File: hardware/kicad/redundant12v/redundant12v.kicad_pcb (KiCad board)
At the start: 2 copper layers, 27 parts, among them J1 Conn_01x06, J2 Conn_02x05_Odd_Even, Q1 2N3904, Q2 2N3904, U1 ATtiny212-SS, U2 MAX232CPE, U3 LD1117S50TR_SOT223, X1 ASCO

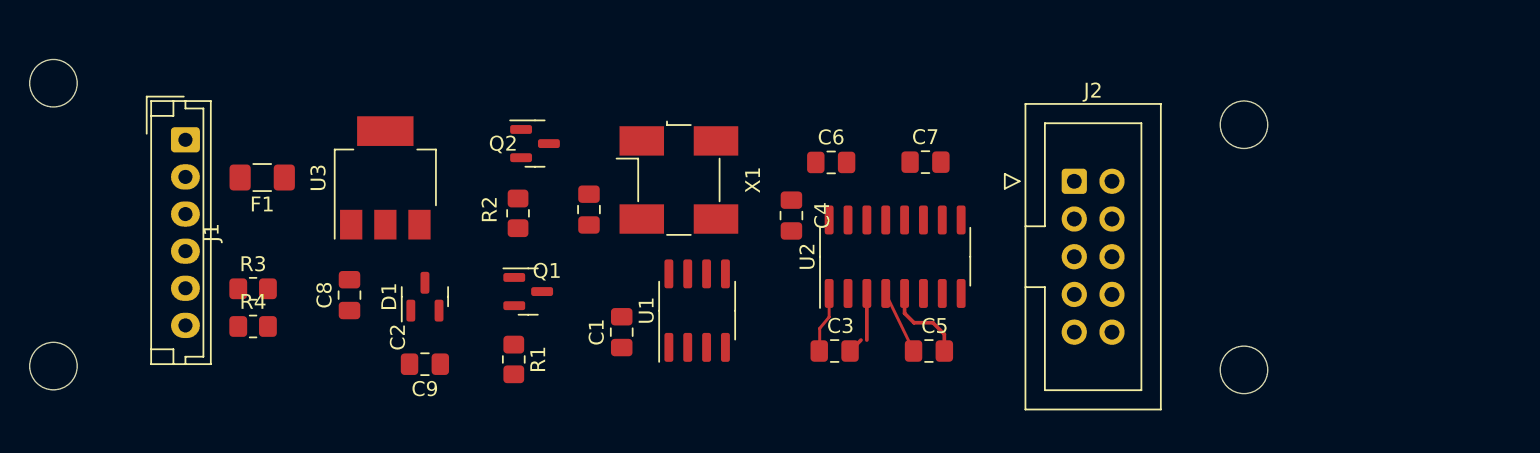
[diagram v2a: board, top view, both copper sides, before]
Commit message: Add serial port connections
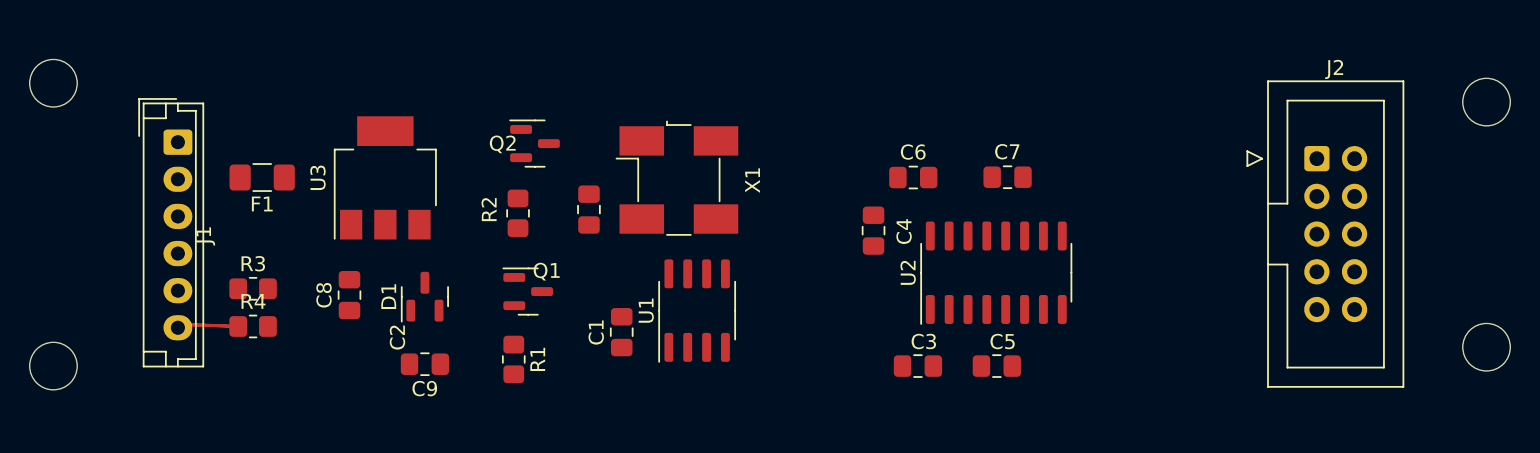
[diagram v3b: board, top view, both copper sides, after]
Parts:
- moved J2 16.4 mm to (189.2, 88.9)
- moved REF** 16.4 mm to (200.7, 85.1)
- moved REF** 16.4 mm to (200.7, 101.6)
- moved U2 6.90 mm to (167.6, 96.6)
- moved C3 5.70 mm to (162.4, 102.9)
- moved C4 5.62 mm to (159.4, 93.7)
- moved C6 5.62 mm to (162.1, 90.2)
- moved C7 5.62 mm to (168.4, 90.2)
- moved C5 4.68 mm to (167.7, 102.9)
- moved J1 0.53 mm to (112.5, 87.8)
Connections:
- net RX renamed RX_5V
- net TX renamed TX_5V
- U2 pad 13: unconnected-(U2-Pad13) -> RX_12V
- U2 pad 14: unconnected-(U2-Pad14) -> TX_12V
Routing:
- net Net-(C5-Pad2): track 5.73 -> 0.00 mm
- net Net-(C3-Pad2): track 4.18 -> 0.00 mm
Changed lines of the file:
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@@
   (net 0 "")
   (net 1 "VCC")
-  (net 2 "TX")
-  (net 3 "RX")
+  (net 2 "TX_5V")
+  (net 3 "RX_5V")
   (net 4 "EXTCLK")
   (net 5 "GND")
@@
   (net 14 "unconnected-(U2-Pad9)")
   (net 15 "unconnected-(U2-Pad10)")
-  (net 16 "unconnected-(U2-Pad13)")
-  (net 17 "unconnected-(U2-Pad14)")
+  (net 16 "RX_12V")
+  (net 17 "TX_12V")
   (net 18 "unconnected-(X1-Pad1)")
   (net 19 "PS0")
@@
   )
   (footprint "Capacitor_SMD:C_0805_2012Metric_Pad1.18x1.45mm_HandSolder" (layer "F.Cu")
-    (at 163.104 101.8545)
+    (at 167.6775 102.87)
     (descr "Capacitor SMD 0805 (2012 Metric), square (rectangular) end terminal, IPC_7351 nominal with elongated pad for handsoldering. (Body size source: IPC-SM-782 page 76, https://www.pcb-3d.com/wordpress/wp-content/uploads/ipc-sm-782a_amendment_1_and_2.pdf, https://docs.google.com/spreadsheets/d/1BsfQQcO9C6DZCsRaXUlFlo91Tg2WpOkGARC1WS5S8t0/edit?usp=sharing), generated with kicad-footprint-generator")
     (tags "capacitor handsolder")
@@
     (property "Sheetname" "")
     (attr smd)
-    (fp_text reference "C5" (at 0.395 -1.68) (layer "F.SilkS")
+    (fp_text reference "C5" (at 0.4105 -1.618) (layer "F.SilkS")
       (effects (font (size 1 1) (thickness 0.15)))
     )
@@
   )
   (footprint "Connector_JST:JST_EH_B6B-EH-A_1x06_P2.50mm_Vertical" (layer "F.Cu")
-    (at 113.03 87.63 -90)
+    (at 112.522 87.79 -90)
     (descr "JST EH series connector, B6B-EH-A (http://www.jst-mfg.com/product/pdf/eng/eEH.pdf), generated with kicad-footprint-generator")
     (tags "connector JST EH vertical")
@@
   )
   (footprint "Capacitor_SMD:C_0805_2012Metric_Pad1.18x1.45mm_HandSolder" (layer "F.Cu")
-    (at 156.5215 89.1545)
+    (at 162.052 90.17)
     (descr "Capacitor SMD 0805 (2012 Metric), square (rectangular) end terminal, IPC_7351 nominal with elongated pad for handsoldering. (Body size source: IPC-SM-782 page 76, https://www.pcb-3d.com/wordpress/wp-content/uploads/ipc-sm-782a_amendment_1_and_2.pdf, https://docs.google.com/spreadsheets/d/1BsfQQcO9C6DZCsRaXUlFlo91Tg2WpOkGARC1WS5S8t0/edit?usp=sharing), generated with kicad-footprint-generator")
     (tags "capacitor handsolder")
@@
       (net 1 "VCC") (pinfunction "VCC") (pintype "power_in"))
     (pad "2" smd roundrect (at -2.475 -0.635 90) (size 1.95 0.6) (layers "F.Cu" "F.Paste" "F.Mask") (roundrect_rratio 0.25)
-      (net 2 "TX") (pinfunction "PA6") (pintype "bidirectional"))
+      (net 2 "TX_5V") (pinfunction "PA6") (pintype "bidirectional"))
     (pad "3" smd roundrect (at -2.475 0.635 90) (size 1.95 0.6) (layers "F.Cu" "F.Paste" "F.Mask") (roundrect_rratio 0.25)
-      (net 3 "RX") (pinfunction "PA7") (pintype "bidirectional"))
+      (net 3 "RX_5V") (pinfunction "PA7") (pintype "bidirectional"))
     (pad "4" smd roundrect (at -2.475 1.905 90) (size 1.95 0.6) (layers "F.Cu" "F.Paste" "F.Mask") (roundrect_rratio 0.25)
       (net 19 "PS0") (pinfunction "PA1") (pintype "bidirectional"))
@@
   )
   (footprint "Package_SO:SOIC-16_3.9x9.9mm_P1.27mm" (layer "F.Cu")
-    (at 160.829 95.5045 90)
+    (at 167.64 96.582 90)
     (descr "SOIC, 16 Pin (JEDEC MS-012AC, https://www.analog.com/media/en/package-pcb-resources/package/pkg_pdf/soic_narrow-r/r_16.pdf), generated with kicad-footprint-generator ipc_gullwing_generator.py")
     (tags "SOIC SO")
@@
       (effects (font (size 1 1) (thickness 0.15)))
     )
-    (fp_text value "MAX232CPE" (at 0 5.9 90) (layer "F.Fab")
+    (fp_text value "MAX232CPE" (at 0 5.9375 90) (layer "F.Fab")
       (effects (font (size 1 1) (thickness 0.15)))
     )
@@
       (net 15 "unconnected-(U2-Pad10)") (pinfunction "T2IN") (pintype "input+no_connect"))
     (pad "11" smd roundrect (at 2.475 1.905 90) (size 1.95 0.6) (layers "F.Cu" "F.Paste" "F.Mask") (roundrect_rratio 0.25)
-      (net 2 "TX") (pinfunction "T1IN") (pintype "input"))
+      (net 2 "TX_5V") (pinfunction "T1IN") (pintype "input"))
     (pad "12" smd roundrect (at 2.475 0.635 90) (size 1.95 0.6) (layers "F.Cu" "F.Paste" "F.Mask") (roundrect_rratio 0.25)
-      (net 3 "RX") (pinfunction "R1OUT") (pintype "output"))
+      (net 3 "RX_5V") (pinfunction "R1OUT") (pintype "output"))
     (pad "13" smd roundrect (at 2.475 -0.635 90) (size 1.95 0.6) (layers "F.Cu" "F.Paste" "F.Mask") (roundrect_rratio 0.25)
-      (net 16 "unconnected-(U2-Pad13)") (pinfunction "R1IN") (pintype "input"))
+      (net 16 "RX_12V") (pinfunction "R1IN") (pintype "input"))
     (pad "14" smd roundrect (at 2.475 -1.905 90) (size 1.95 0.6) (layers "F.Cu" "F.Paste" "F.Mask") (roundrect_rratio 0.25)
-      (net 17 "unconnected-(U2-Pad14)") (pinfunction "T1OUT") (pintype "output"))
+      (net 17 "TX_12V") (pinfunction "T1OUT") (pintype "output"))
     (pad "15" smd roundrect (at 2.475 -3.175 90) (size 1.95 0.6) (layers "F.Cu" "F.Paste" "F.Mask") (roundrect_rratio 0.25)
       (net 5 "GND") (pinfunction "GND") (pintype "power_in"))
@@
   )
   (footprint "MountingHole:MountingHole_3.2mm_M3" (layer "F.Cu")
-    (at 184.324 86.6145)
+    (at 200.66 85.09)
     (descr "Mounting Hole 3.2mm, no annular, M3")
     (tags "mounting hole 3.2mm no annular m3")
@@
   )
   (footprint "MountingHole:MountingHole_3.2mm_M3" (layer "F.Cu")
-    (at 184.324 103.1245)
+    (at 200.66 101.6)
     (descr "Mounting Hole 3.2mm, no annular, M3")
     (tags "mounting hole 3.2mm no annular m3")
@@
   )
   (footprint "Capacitor_SMD:C_0805_2012Metric_Pad1.18x1.45mm_HandSolder" (layer "F.Cu")
-    (at 156.754 101.8545)
+    (at 162.365 102.87)
     (descr "Capacitor SMD 0805 (2012 Metric), square (rectangular) end terminal, IPC_7351 nominal with elongated pad for handsoldering. (Body size source: IPC-SM-782 page 76, https://www.pcb-3d.com/wordpress/wp-content/uploads/ipc-sm-782a_amendment_1_and_2.pdf, https://docs.google.com/spreadsheets/d/1BsfQQcO9C6DZCsRaXUlFlo91Tg2WpOkGARC1WS5S8t0/edit?usp=sharing), generated with kicad-footprint-generator")
     (tags "capacitor handsolder")
@@
     (property "Sheetname" "")
     (attr smd)
-    (fp_text reference "C3" (at 0.395 -1.68) (layer "F.SilkS")
+    (fp_text reference "C3" (at 0.4105 -1.618) (layer "F.SilkS")
       (effects (font (size 1 1) (thickness 0.15)))
     )
@@
   )
   (footprint "Capacitor_SMD:C_0805_2012Metric_Pad1.18x1.45mm_HandSolder" (layer "F.Cu")
-    (at 153.844 92.732 -90)
+    (at 159.3745 93.7475 -90)
     (descr "Capacitor SMD 0805 (2012 Metric), square (rectangular) end terminal, IPC_7351 nominal with elongated pad for handsoldering. (Body size source: IPC-SM-782 page 76, https://www.pcb-3d.com/wordpress/wp-content/uploads/ipc-sm-782a_amendment_1_and_2.pdf, https://docs.google.com/spreadsheets/d/1BsfQQcO9C6DZCsRaXUlFlo91Tg2WpOkGARC1WS5S8t0/edit?usp=sharing), generated with kicad-footprint-generator")
     (tags "capacitor handsolder")
@@
     (property "Sheetname" "")
     (attr smd)
-    (fp_text reference "C4" (at 0 -2.075 90) (layer "F.SilkS")
-      (effects (font (size 1 1) (thickness 0.15)))
-    )
-    (fp_text value "C_Small" (at -1.25 -3.17 90) (layer "F.Fab")
+    (fp_text reference "C4" (at 0.062 -2.0905 90) (layer "F.SilkS")
+      (effects (font (size 1 1) (thickness 0.15)))
+    )
+    (fp_text value "C_Small" (at -1.188 -3.1855 90) (layer "F.Fab")
       (effects (font (size 1 1) (thickness 0.15)))
     )
@@
   )
   (footprint "Capacitor_SMD:C_0805_2012Metric_Pad1.18x1.45mm_HandSolder" (layer "F.Cu")
-    (at 162.8715 89.1345)
+    (at 168.402 90.15)
     (descr "Capacitor SMD 0805 (2012 Metric), square (rectangular) end terminal, IPC_7351 nominal with elongated pad for handsoldering. (Body size source: IPC-SM-782 page 76, https://www.pcb-3d.com/wordpress/wp-content/uploads/ipc-sm-782a_amendment_1_and_2.pdf, https://docs.google.com/spreadsheets/d/1BsfQQcO9C6DZCsRaXUlFlo91Tg2WpOkGARC1WS5S8t0/edit?usp=sharing), generated with kicad-footprint-generator")
     (tags "capacitor handsolder")
@@
       (effects (font (size 1 1) (thickness 0.15)))
     )
-    (fp_text value "C_Small" (at 0.395 1.68) (layer "F.Fab")
+    (fp_text value "C_Small" (at 2.7755 1.742) (layer "F.Fab")
       (effects (font (size 1 1) (thickness 0.15)))
     )
@@
   )
   (footprint "Connector_IDC:IDC-Header_2x05_P2.54mm_Vertical" (layer "F.Cu")
-    (at 172.894 90.4245)
+    (at 189.23 88.9)
     (descr "Through hole IDC box header, 2x05, 2.54mm pitch, DIN 41651 / IEC 60603-13, double rows, https://docs.google.com/spreadsheets/d/16SsEcesNF15N3Lb4niX7dcUr-NY5_MFPQhobNuNppn4/edit#gid=0")
     (tags "Through hole vertical IDC box header THT 2x05 2.54mm double row")
@@
     )
   )
-  (gr_line (start 156.384 99.5685) (end 155.749 100.3305) (layer "F.Cu") (width 0.2))
-  (gr_line (start 160.194 97.9937) (end 162.0736 101.8545) (layer "F.Cu") (width 0.2))
-  (gr_line (start 156.384 98.0445) (end 156.384 99.5685) (layer "F.Cu") (width 0.2))
-  (gr_line (start 155.749 100.3305) (end 155.749 101.8545) (layer "F.Cu") (width 0.2))
-  (segment (start 157.7915 101.8545) (end 158.529 101.117) (width 0.25) (layer "F.Cu") (net 8))
-  (segment (start 158.924 101.117) (end 158.924 97.9795) (width 0.25) (layer "F.Cu") (net 8))
-  (segment (start 163.369 99.9495) (end 164.1415 100.722) (width 0.25) (layer "F.Cu") (net 10))
-  (segment (start 161.464 99.3145) (end 162.099 99.9495) (width 0.25) (layer "F.Cu") (net 10))
-  (segment (start 162.099 99.9495) (end 163.369 99.9495) (width 0.25) (layer "F.Cu") (net 10))
-  (segment (start 164.1415 101.8545) (end 164.1415 100.722) (width 0.25) (layer "F.Cu") (net 10))
-  (segment (start 161.464 97.9795) (end 161.464 99.3145) (width 0.25) (layer "F.Cu") (net 10))
+  (gr_line (start 113.03 100.076) (end 116.713 100.203) (layer "F.Cu") (width 0.2))
+  (gr_line (start 113.03 100.076) (end 116.713 100.203) (layer "F.Cu") (width 0.2))
 )

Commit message: PCB is mostly routed
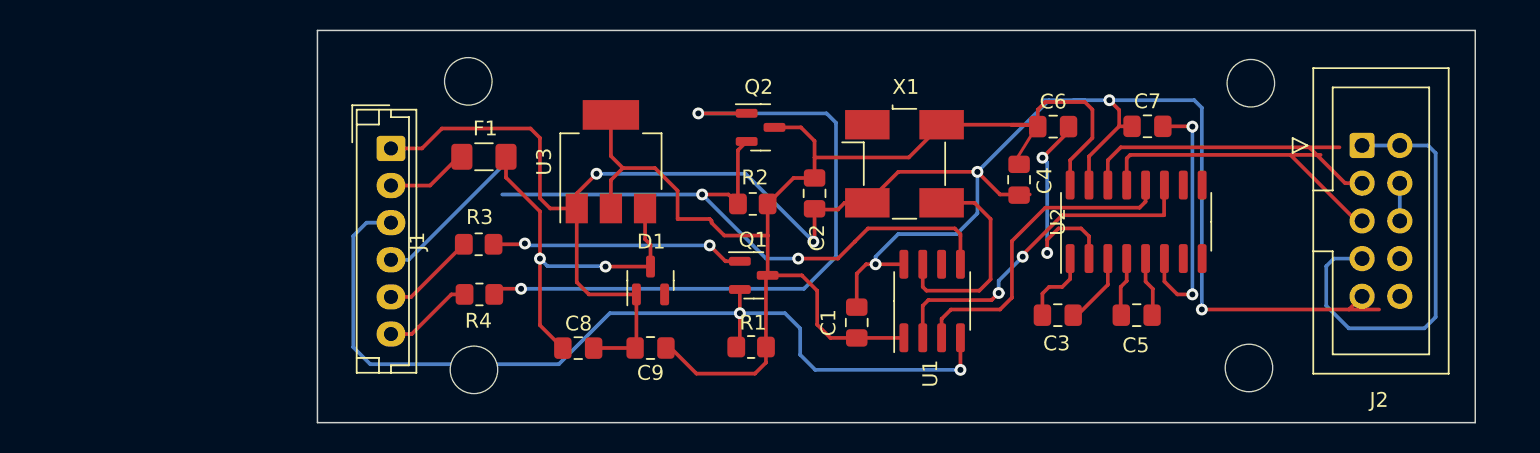
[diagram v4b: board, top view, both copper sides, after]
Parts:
- J2: value Conn_02x05_Odd_Even -> IDC 2x5 Male
- R3, R4: value 100 -> 150
- moved REF** 28.3 mm to (132.5, 103.1)
- moved REF** 27.9 mm to (132.1, 83.7)
- moved REF** 16.1 mm to (184.7, 103.0)
- moved R1 16.0 mm to (151.1, 101.6), turned to 180 degrees
- moved REF** 15.9 mm to (184.8, 83.8)
- moved C1 15.8 mm to (158.2, 99.9), turned to -90 degrees
- moved U1 15.8 mm to (163.3, 98.5)
- moved R2 15.8 mm to (151.2, 91.9), turned to 180 degrees
- moved C8 15.8 mm to (139.5, 101.7), turned to 180 degrees
- moved R3 15.5 mm to (132.8, 94.7), turned to 180 degrees
- moved R4 15.4 mm to (132.8, 98.0), turned to 180 degrees
- moved C2 15.2 mm to (155.4, 91.2)
- moved C9 15.2 mm to (144.4, 101.7)
- moved D1 15.2 mm to (144.4, 97.1)
- moved Q2 15.2 mm to (151.8, 86.8)
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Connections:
- J2 pad 1: unconnected-(J2-Pad1) -> Net-(J2-Pad1)
- J2 pad 2: unconnected-(J2-Pad2) -> Net-(J2-Pad1)
- J2 pad 3: unconnected-(J2-Pad3) -> TX_12V
- J2 pad 4: unconnected-(J2-Pad4) -> Net-(J2-Pad4)
- J2 pad 5: unconnected-(J2-Pad5) -> RX_12V
- J2 pad 6: unconnected-(J2-Pad6) -> Net-(J2-Pad4)
- J2 pad 7: unconnected-(J2-Pad7) -> Net-(J2-Pad1)
- J2 pad 9: unconnected-(J2-Pad9) -> GND
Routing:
- net GND: track 0.00 -> 141.3 mm, vias 0 -> 6
- net VCC: track 0.00 -> 88.1 mm
- net PS0: track 0.00 -> 61.9 mm, vias 0 -> 2
- net PS1: track 0.00 -> 52.9 mm, vias 0 -> 2
- net Net-(Q2-Pad1): track 0.00 -> 45.9 mm, vias 0 -> 2
- net Net-(J2-Pad1): track 0.00 -> 29.8 mm
- net Net-(C8-Pad2): track 0.00 -> 26.2 mm, vias 0 -> 2
- net TX_5V: track 0.00 -> 23.9 mm, vias 0 -> 2
- net TX_12V: track 0.00 -> 22.2 mm
- net RX_5V: track 0.00 -> 21.6 mm
- net RX_12V: track 0.00 -> 20.7 mm
- net Net-(Q1-Pad1): track 0.00 -> 17.1 mm, vias 0 -> 2
- net Net-(C7-Pad2): track 0.00 -> 17.1 mm, vias 0 -> 2
- net Net-(C6-Pad2): track 0.00 -> 15.7 mm, vias 0 -> 2
- net EXTCLK: track 0.00 -> 14.3 mm
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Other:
- board outline added: 78 x 26.4 mm

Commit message: PCB rev 1 finished
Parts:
- added TP1: GND, TestPoint:TestPoint_Pad_D2.5mm, B.Cu at (143.3, 103.6)
- added TP1: VTG_5V, TestPoint:TestPoint_Pad_D2.5mm, B.Cu at (149.4, 103.6)
- added TP2: UPDI, TestPoint:TestPoint_Pad_D2.5mm, B.Cu at (155.3, 103.6)
- moved J2 14.4 mm to (177.9, 88.0)
- moved REF** 14.1 mm to (170.7, 83.9)
- moved REF** 14.0 mm to (170.7, 103.1)
- moved C5 12.0 mm to (165.5, 102.4), turned to -90 degrees
- moved C7 11.2 mm to (166.6, 87.6), turned to 90 degrees
- moved U2 9.49 mm to (167.9, 95.7)
- moved C3 9.31 mm to (162.9, 102.4), turned to -90 degrees
- moved C6 9.08 mm to (162.4, 87.6), turned to -90 degrees
- moved C1 6.10 mm to (152.1, 100.0)
- moved U1 6.10 mm to (157.2, 98.5)
- moved C4 5.32 mm to (164.6, 87.6)
- moved X1 4.57 mm to (156.9, 89.3)
- moved C2 4.06 mm to (151.3, 91.3)
- moved Q2 3.13 mm to (148.6, 86.8)
- moved R2 3.13 mm to (148.1, 92.0)
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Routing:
- net GND: track 141.3 -> 111.7 mm, vias 6 -> 7
- net UPDI: track 0.00 -> 16.9 mm, vias 0 -> 1
- net Net-(Q2-Pad1): track 45.9 -> 33.7 mm
- net VCC: track 88.1 -> 77.3 mm, vias 0 -> 1
- net TX_12V: track 22.2 -> 14.5 mm
- net RX_12V: track 20.7 -> 13.1 mm
- net PS1: track 52.9 -> 45.9 mm
- net PS0: track 61.9 -> 55.9 mm
- net Net-(C6-Pad2): track 15.7 -> 10.6 mm
- net RX_5V: track 21.6 -> 17.1 mm
- net Net-(C8-Pad2): track 26.2 -> 23.0 mm
- net Net-(Q1-Pad1): track 17.1 -> 14.2 mm
- net Net-(C5-Pad2): track 4.03 -> 6.94 mm
- net Net-(C3-Pad2): track 4.94 -> 7.61 mm
- net Net-(C7-Pad2): track 17.1 -> 15.3 mm
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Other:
- board size 78 x 26.4 mm -> 66.7 x 26.4 mm
- board text added: "12V"
- board text added: "CTS"
- board text added: "DCD"
- board text added: "DSR"
- board text added: "DTR"
- board text added: "GND"
- board text added: "LED0+"
- board text added: "LED1+"
- board text added: "NC"
- board text added: "PS0"
- board text added: "PS1"
- board text added: "REDUNDANT 12V MONITOR REV. 1"
- board text added: "RI"
- board text added: "RTS"
- board text added: "RX"
- board text added: "TX"
- board text added: "UPDI"
- board text added: "VTG_5V"
- board text added: "© 2022 M. NABEREZNY"
